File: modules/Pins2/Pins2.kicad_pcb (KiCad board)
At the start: 2 copper layers, 40.6 x 40.6 mm, 34 parts, among them J1 2, J10 11, J11 12, J12 13, J13 A0, J14 A1, J15 A2, J16 A3, J17 A4, J18 A5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

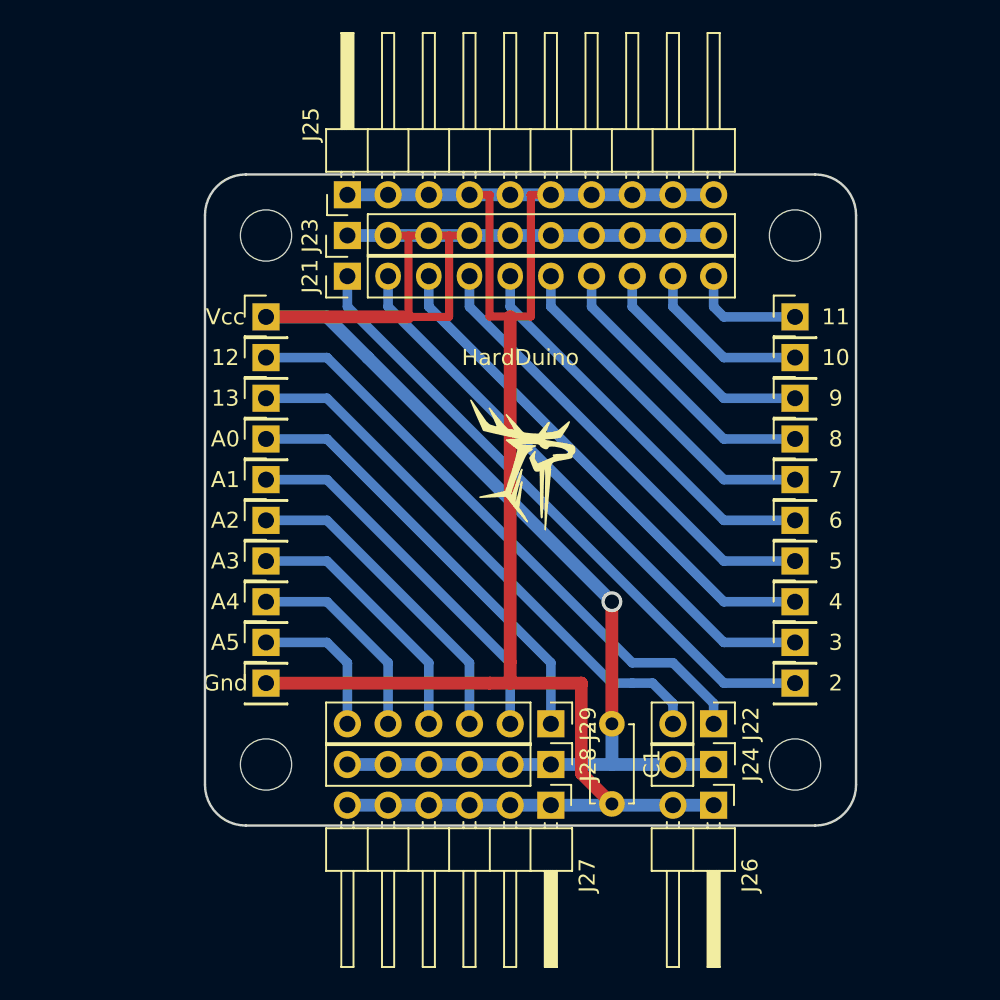
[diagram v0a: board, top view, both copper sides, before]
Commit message: 1x PCBs. Move holes to edges. Caution! This changes is uncompatible with previous versions...
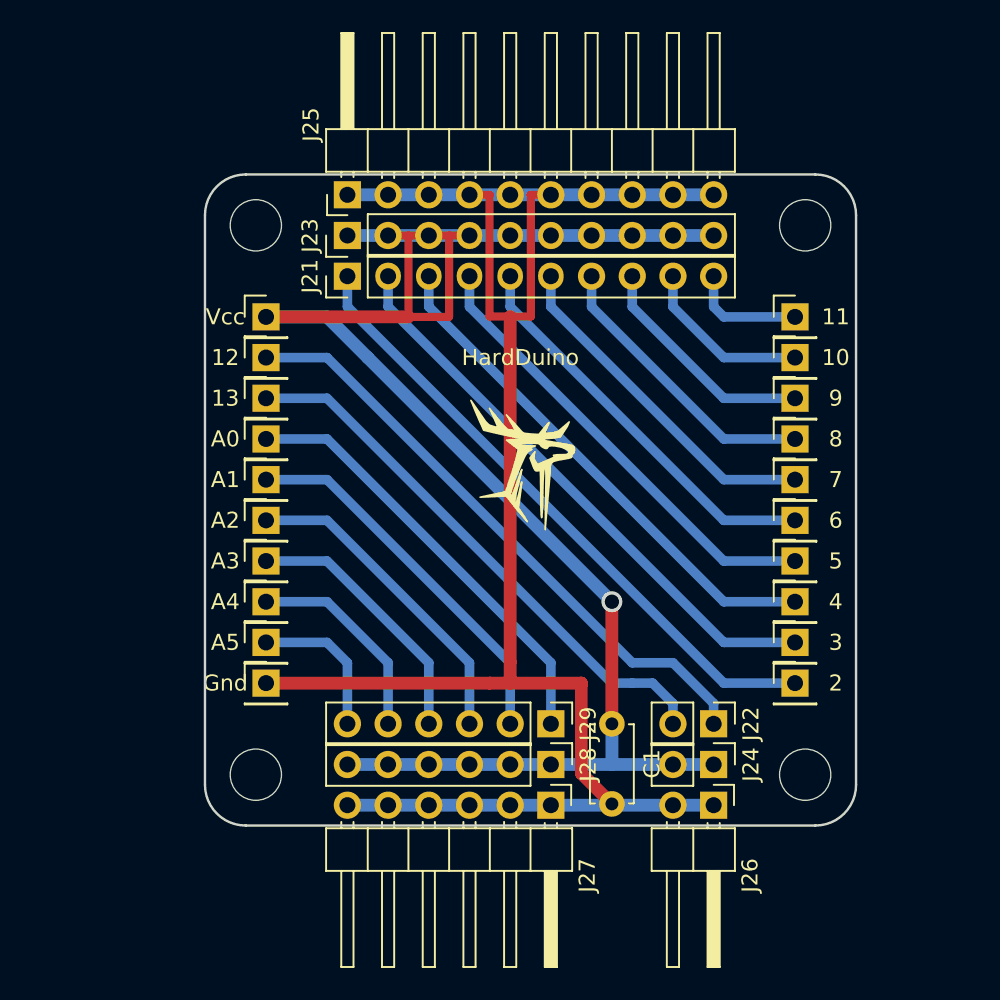
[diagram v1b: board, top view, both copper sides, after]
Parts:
- moved H2 0.90 mm to (92.1, 88.3)
- moved H4 0.90 mm to (126.4, 88.3)
- moved H1 0.90 mm to (92.1, 54.0)
- moved H3 0.90 mm to (126.4, 54.0)
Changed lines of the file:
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@@
   )
   (module MountingHole:MountingHole_3.2mm_M3 (layer F.Cu)
-    (at 92.71 54.61)
+    (at 92.0750 53.9750)
     (descr "Mounting Hole 3.2mm, no annular, M3")
     (tags "mounting hole 3.2mm no annular m3")
@@
   )
   (module MountingHole:MountingHole_3.2mm_M3 (layer F.Cu)
-    (at 92.71 87.63)
+    (at 92.0750 88.2650)
     (descr "Mounting Hole 3.2mm, no annular, M3")
     (tags "mounting hole 3.2mm no annular m3")
@@
   )
   (module MountingHole:MountingHole_3.2mm_M3 (layer F.Cu)
-    (at 125.73 54.61)
+    (at 126.3650 53.9750)
     (descr "Mounting Hole 3.2mm, no annular, M3")
     (tags "mounting hole 3.2mm no annular m3")
@@
   )
   (module MountingHole:MountingHole_3.2mm_M3 (layer F.Cu)
-    (at 125.73 87.63)
+    (at 126.3650 88.2650)
     (descr "Mounting Hole 3.2mm, no annular, M3")
     (tags "mounting hole 3.2mm no annular m3")

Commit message: All 1x shields was rotated clockwise
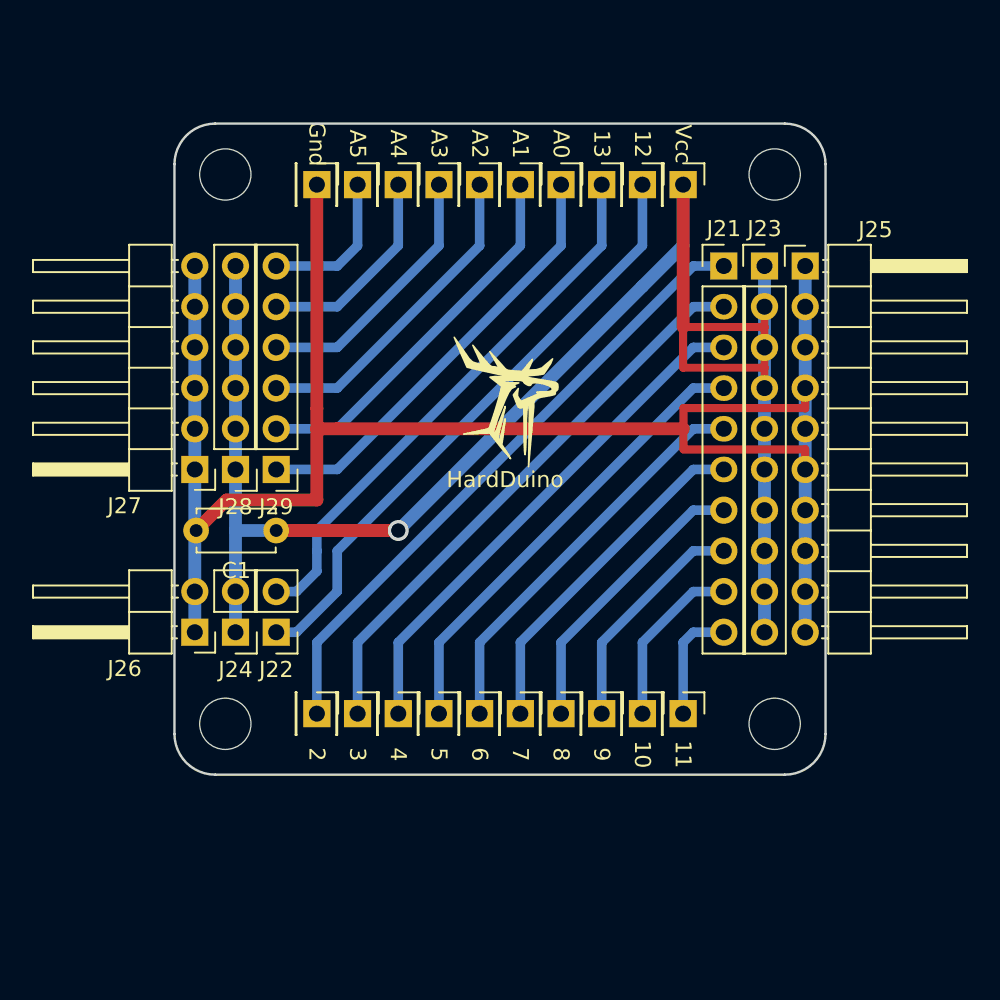
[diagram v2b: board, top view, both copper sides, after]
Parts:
- moved H2 37.5 mm to (90.2, 50.8), turned to 270 degrees
- moved H4 36.3 mm to (90.2, 85.1), turned to 270 degrees
- moved J26 34.1 mm to (88.3, 79.4), turned to 180 degrees
- moved H1 32.5 mm to (124.5, 50.8), turned to 270 degrees
- moved J20 31.3 mm to (95.9, 51.4), turned to 270 degrees
- moved H3 31.2 mm to (124.5, 85.1), turned to 270 degrees
- moved J24 31.0 mm to (90.8, 79.4), turned to 180 degrees
- moved J27 30.5 mm to (88.3, 69.2), turned to 180 degrees
- moved J1 29.9 mm to (95.9, 84.5), turned to 270 degrees
- moved J18 29.1 mm to (98.4, 51.4), turned to 270 degrees
- moved J25 28.9 mm to (126.4, 56.5), turned to 0 degrees
- moved J22 27.9 mm to (93.3, 79.4), turned to 180 degrees
- moved J2 27.7 mm to (98.4, 84.5), turned to 270 degrees
- moved J19 27.3 mm to (118.7, 51.4), turned to 270 degrees
- moved J17 27.3 mm to (101.0, 51.4), turned to 270 degrees
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
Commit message: Now all mounting holes have distance 31.92 x 31.1
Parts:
- moved H2 1.99 mm to (91.4, 52.4), turned to 0 degrees
- moved H4 1.99 mm to (91.4, 83.5), turned to 0 degrees
- moved H1 1.99 mm to (123.3, 52.4), turned to 0 degrees
- moved H3 1.99 mm to (123.3, 83.5), turned to 0 degrees
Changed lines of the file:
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@@
   )
   (module MountingHole:MountingHole_3.2mm_M3 (layer F.Cu)
-    (at 124.46 50.8 270)
+    (at 123.2750 52.3950)
     (descr "Mounting Hole 3.2mm, no annular, M3")
     (tags "mounting hole 3.2mm no annular m3")
@@
   )
   (module MountingHole:MountingHole_3.2mm_M3 (layer F.Cu)
-    (at 90.17 50.8 270)
+    (at 91.3550 52.3950)
     (descr "Mounting Hole 3.2mm, no annular, M3")
     (tags "mounting hole 3.2mm no annular m3")
@@
   )
   (module MountingHole:MountingHole_3.2mm_M3 (layer F.Cu)
-    (at 124.46 85.09 270)
+    (at 123.2750 83.4950)
     (descr "Mounting Hole 3.2mm, no annular, M3")
     (tags "mounting hole 3.2mm no annular m3")
@@
   )
   (module MountingHole:MountingHole_3.2mm_M3 (layer F.Cu)
-    (at 90.17 85.09 270)
+    (at 91.3550 83.4950)
     (descr "Mounting Hole 3.2mm, no annular, M3")
     (tags "mounting hole 3.2mm no annular m3")
